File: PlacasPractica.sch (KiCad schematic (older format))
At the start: 70 parts

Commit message: Añadidos puertos
Puertos comunicaciones y sensores
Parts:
- removed 1M, 3M, R? (x6): R, symbol R
- removed C? (x5): CP, symbol CP
- removed C? (x4): C, symbol C
- removed D? (x2): D_Schottky, symbol D_Schottky
- removed D? (x3): D_Schottky_Small, symbol D_Schottky_Small
- removed J?: CONN_01X03_FEMALE, symbol CONN_01X03_FEMALE
- removed J? (x2): CONN_01X02_MALE, symbol CONN_01X02_MALE
- removed JP? (x2): Jumper_NC_Dual, symbol Jumper_NC_Dual
- removed Q? (x3): Q_PMOS_GDS, symbol Q_PMOS_GDS
- removed U?: MCP73831T-2ATI/OT, SOT95P300X145-5N, symbol MCP73831T-2ATI/OT
- removed U? (x3): XC6220B331MR-G, SOT95P300X145-5N, symbol XC6220B331MR-G
- added ADC? (x2), DIGITAL? (x2), ONEWIRE?: CONN_01x04, symbol CONN_01x04
- added C? (x3): C, symbol C
- added C? (x3): CP, symbol CP
- added D? (x3): D_Schottky_Small, symbol D_Schottky_Small
- added JP? (x2): Jumper_NC_Dual, symbol Jumper_NC_Dual
- added R? (x2): R, symbol R
- added U? (x3): XC6220B331MR-G, SOT95P300X145-5N, symbol XC6220B331MR-G
- renumbered 0.1uF to 0.1uF?, 4k7 to 4k?, i2c to I2C?, UART to UART?
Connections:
- net 3V3_SW is gone; now on net SCL: I2C?.1
- net 3v3_SW is gone; now on net OneWire: R?.1
- net +5V: now also D?.2 (A), D?.2 (A), D?.2 (A)
- net 3v3: no longer UART?.1
- net A0: now also ADC?.2
- net A1: now also ADC?.2
- net D0: now also DIGITAL?.2
- net D1: now also DIGITAL?.1
- net D2: now also DIGITAL?.2
- net D3: now also DIGITAL?.1
- net GND: now also D?.1 (K), I2C?.4, ADC?.4, ADC?.4, C?.2, C?.2, C?.2, C?.2, C?.2, C?.2, DIGITAL?.4, DIGITAL?.4, ONEWIRE?.4, R?.2, R?.2, U?.2 (GND), U?.2 (GND), U?.2 (GND); no longer I2C?.2
- net OneWire: now also U?.35 (GCLKIO2/TC2WO0/SERCOM3P0/SERCOM1P0/X4/PA16), ONEWIRE?.2; no longer R?.2
- net RXD: now also UART?.1; no longer UART?.3
- net SCL: no longer I2C?.3
- net SDA: now also I2C?.2; no longer I2C?.4
- net VCC_COM: now reaches U?.38 (ACCMP1/TC3WO1/SERCOM3P3/SERCOM1P3/X7/PA19)
- net VCC_COM: now also JP?.1
- net at JP?.1: now also R?.2
- net at R?.1: now also D?.2 (A); no longer JP?.2
- net 3v3_BEE renamed 3V3_COM
- net 3V3_COM: now also UART?.3, C?.1, DIGITAL?.3, DIGITAL?.3, U?.5 (VOUT)
- net BAT_VOLT: no longer names the net of U?.61 (PB00/AIN8/Y6/SERCOM5P2/TC7WO0)
- net BEE_VCC: no longer names the net of U?.53 (GCLKIO0/PA28)
- net VCC_SW renamed VCC_SENS
- net VCC_SENS: now also JP?.1
- new net: C?.1, D?.1 (K), JP?.2, U?.1 (VIN), U?.3 (CE)
- new net: C?.1, D?.1 (K), JP?.3, U?.1 (VIN) (x2)
- new net: JP?.2, R?.1, U?.3 (CE) (x2)
- new net 3V3: C?.1, U?.5 (VOUT)
- new net 3V3_SENS: ADC?.3, ADC?.3, C?.1, I2C?.3, ONEWIRE?.3, R?.2, U?.5 (VOUT)
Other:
- note added: "COMMUNICATION SWITCH"
- note added: "GENERAL 3V3"
- note added: "SENSOR SWITCH"
- note removed: "3v3"
- note removed: "BATT/SOLAR"
- note removed: "BEE SWITCH"
- note removed: "I/O SWITCH"
- note removed: "LiPo CHARGER"
- moved on the sheet: 0.1uF?, 4k?, D?, I2C?, J?, JP?, R?, U?, UART?

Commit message: Reset, Vddcore
Se  ha añadido el botón de reset y el jumper para la conexión de Vddcore en función del chip a usar.
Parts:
- added C?: 100nF, symbol C
- added JP?: Jumper_NC_Dual, symbol Jumper_NC_Dual
- added R?: 330, symbol R
- added R?: 10k, symbol R
- added SW?: SW_Push, symbol SW_Push
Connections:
- net 3V3: now also R?.1
- net GND: now also C?.2, SW?.2
- net RESETN: now also C?.1, R?.1, R?.2
- net Vddcore2: now reaches U?.53 (GCLKIO0/PA28)
- net Vddcore2: now also JP?.1
- net at C?.1: now also JP?.2; no longer U?.55 (VDDCORE)
- new net: R?.2, SW?.1
- new net Vddcore1: JP?.3, U?.55 (VDDCORE)
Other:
- note added: "Para D21\n"
- note added: "Para L21"
- note added: "Reset_button\n"
- note added: "Vddcore"
- moved on the sheet: C?
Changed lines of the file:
@@
 LIBS:contrib
 LIBS:valves
+LIBS:switches
 LIBS:PlacasPractica-cache
 EELAYER 25 0
@@
 L CP C?
 U 1 1 59060D19
-P 2050 1600
-F 0 "C?" H 2075 1700 50  0000 L CNN
-F 1 "CP" H 2075 1500 50  0000 L CNN
-F 2 "" H 2088 1450 50  0001 C CNN
-F 3 "" H 2050 1600 50  0001 C CNN
-	1    2050 1600
+P 9800 4800
+F 0 "C?" H 9825 4900 50  0000 L CNN
+F 1 "CP" H 9825 4700 50  0000 L CNN
+F 2 "" H 9838 4650 50  0001 C CNN
+F 3 "" H 9800 4800 50  0001 C CNN
+	1    9800 4800
 	-1   0    0    1
 $EndComp
@@
 L GND #PWR?
 U 1 1 59060D29
-P 2050 1400
-F 0 "#PWR?" H 2050 1150 50  0001 C CNN
-F 1 "GND" H 2050 1250 50  0000 C CNN
-F 2 "" H 2050 1400 50  0001 C CNN
-F 3 "" H 2050 1400 50  0001 C CNN
-	1    2050 1400
+P 9800 4600
+F 0 "#PWR?" H 9800 4350 50  0001 C CNN
+F 1 "GND" H 9800 4450 50  0000 C CNN
+F 2 "" H 9800 4600 50  0001 C CNN
+F 3 "" H 9800 4600 50  0001 C CNN
+	1    9800 4600
 	-1   0    0    1
 $EndComp
@@
 xBEE COM
 Wire Wire Line
-	2050 1400 2050 1450
+	9800 4600 9800 4650
 Wire Wire Line
 	2050 1750 2050 1800
@@
 Text Label 4400 3700 0    60   ~ 0
 OneWire
+$Comp
+L SW_Push SW?
+U 1 1 5AB3F66E
+P 7100 5850
+F 0 "SW?" H 7150 5950 50  0000 L CNN
+F 1 "SW_Push" H 7100 5790 50  0000 C CNN
+F 2 "" H 7100 6050 50  0001 C CNN
+F 3 "" H 7100 6050 50  0001 C CNN
+	1    7100 5850
+	0    1    1    0
+$EndComp
+$Comp
+L R R?
+U 1 1 5AB3FDE9
+P 7100 5350
+F 0 "R?" V 7180 5350 50  0000 C CNN
+F 1 "330" V 7100 5350 50  0000 C CNN
+F 2 "" V 7030 5350 50  0001 C CNN
+F 3 "" H 7100 5350 50  0001 C CNN
+	1    7100 5350
+	1    0    0    -1
+$EndComp
+$Comp
+L R R?
+U 1 1 5AB3FE8C
+P 7450 4700
+F 0 "R?" V 7530 4700 50  0000 C CNN
+F 1 "10k" V 7450 4700 50  0000 C CNN
+F 2 "" V 7380 4700 50  0001 C CNN
+F 3 "" H 7450 4700 50  0001 C CNN
+	1    7450 4700
+	1    0    0    -1
+$EndComp
+$Comp
+L C C?
+U 1 1 5AB3FF4F
+P 7700 5350
+F 0 "C?" H 7725 5450 50  0000 L CNN
+F 1 "100nF" H 7725 5250 50  0000 L CNN
+F 2 "" H 7738 5200 50  0001 C CNN
+F 3 "" H 7700 5350 50  0001 C CNN
+	1    7700 5350
+	1    0    0    -1
+$EndComp
+$Comp
+L GND #PWR?
+U 1 1 5AB40006
+P 7700 6100
+F 0 "#PWR?" H 7700 5850 50  0001 C CNN
+F 1 "GND" H 7700 5950 50  0000 C CNN
+F 2 "" H 7700 6100 50  0001 C CNN
+F 3 "" H 7700 6100 50  0001 C CNN
+	1    7700 6100
+	1    0    0    -1
+$EndComp
+$Comp
+L GND #PWR?
+U 1 1 5AB40094
+P 8050 6100
+F 0 "#PWR?" H 8050 5850 50  0001 C CNN
+F 1 "GND" H 8050 5950 50  0000 C CNN
+F 2 "" H 8050 6100 50  0001 C CNN
+F 3 "" H 8050 6100 50  0001 C CNN
+	1    8050 6100
+	0    -1   -1   0
+$EndComp
+Wire Wire Line
+	7450 4850 7450 5200
+Wire Wire Line
+	7100 5200 8150 5200
+Connection ~ 7450 5200
+Wire Wire Line
+	7100 5500 7100 5650
+Wire Wire Line
+	7100 6050 7100 6100
+Wire Wire Line
+	7100 6100 8050 6100
+Connection ~ 7700 6100
+Wire Wire Line
+	7700 5500 7700 6100
+Text Label 7450 4550 1    60   ~ 0
+3V3
+Connection ~ 7700 5200
+Text Label 8150 5200 0    60   ~ 0
+RESETN
+Wire Notes Line
+	6700 4250 6700 6450
+Wire Notes Line
+	6700 6450 8650 6450
+Wire Notes Line
+	8650 6450 8650 4250
+Wire Notes Line
+	8650 4250 6700 4250
+Text Notes 7750 4550 0    60   ~ 0
+Reset_button\n
+Text Label 2050 1750 1    60   ~ 0
+Vddcore1
+Text Label 9550 5150 2    60   ~ 0
+Vddcore1
+Text Label 10100 5150 0    60   ~ 0
+Vddcore2
+$Comp
+L Jumper_NC_Dual JP?
+U 1 1 5AB4AF6E
+P 9800 5150
+F 0 "JP?" H 9850 5050 50  0000 L CNN
+F 1 "Jumper_NC_Dual" H 9800 5250 50  0000 C BNN
+F 2 "" H 9800 5150 50  0001 C CNN
+F 3 "" H 9800 5150 50  0001 C CNN
+	1    9800 5150
+	-1   0    0    1
+$EndComp
+Wire Wire Line
+	10100 5150 10050 5150
+Wire Wire Line
+	9800 4950 9800 5050
+Text Label 4400 4800 0    60   ~ 0
+Vddcore2
+Wire Notes Line
+	9000 4250 9000 5650
+Wire Notes Line
+	9000 5650 10650 5650
+Wire Notes Line
+	10650 5650 10650 4250
+Wire Notes Line
+	10650 4250 9000 4250
+Text Notes 10050 4500 0    60   ~ 0
+Vddcore
+Text Notes 10100 4950 0    60   ~ 0
+Para L21
+Text Notes 9150 5000 0    60   ~ 0
+Para D21\n
 $EndSCHEMATC

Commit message: Añadidos conectores genericos
Se han añadido los conectores genéricos
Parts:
- added J? (x2): Conn_01x10, symbol Conn_01x10
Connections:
- net 3V3: now also J?.2 (Pin_2), J?.9 (Pin_9)
- net A2: now also J?.3 (Pin_3)
- net A3: now also J?.4 (Pin_4)
- net A4: now also J?.5 (Pin_5)
- net A5: now also J?.6 (Pin_6)
- net A6: now also J?.7 (Pin_7)
- net A7: now also J?.8 (Pin_8)
- net A8: now also J?.9 (Pin_9)
- net A9: now also J?.10 (Pin_10)
- net D10: now also J?.2 (Pin_2)
- net D4: now also J?.8 (Pin_8)
- net D5: now also J?.7 (Pin_7)
- net D6: now also J?.6 (Pin_6)
- net D7: now also J?.5 (Pin_5)
- net D8: now also J?.4 (Pin_4)
- net D9: now also J?.3 (Pin_3)
- net GND: now also J?.1 (Pin_1), J?.10 (Pin_10)
- net D12: now reaches U?.36 (GCLKIO3/TC2WO1/SERCOM3P1/SERCOM1P1/X5/PA17)
- net D13: now reaches U?.37 (ACCMP0/TC3WO0/SERCOM3P2/SERCOM1P2/X6/PA18)
- net OneWire renamed D11
- net D11: now also J?.1 (Pin_1)
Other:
- note added: "CONECTORES DEDICADOS"
- note added: "CONECTORES GENERICOS"
- note removed: "CONECTORES"
- moved on the sheet: C?, JP?, R?, SW?

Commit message: Actualizado anotado
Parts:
- gave numbers to parts that had none: 64

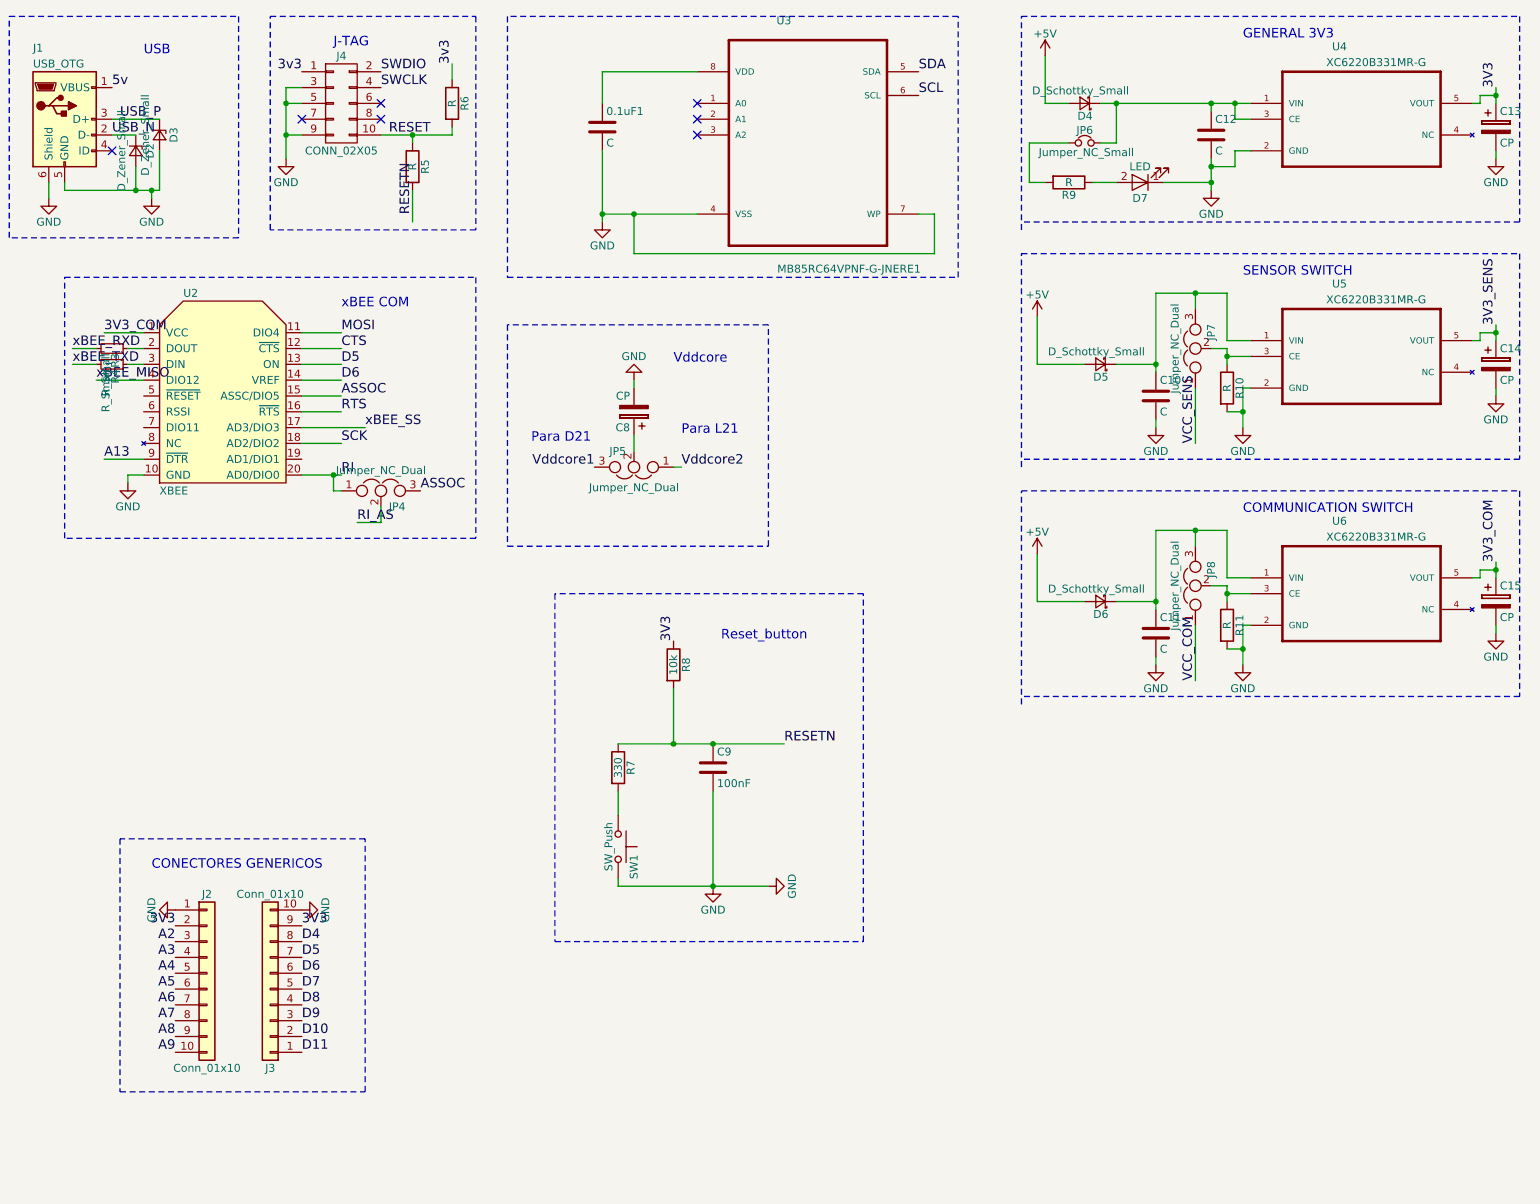
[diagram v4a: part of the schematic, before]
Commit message: Modificacion de la alimentación de Vddcore
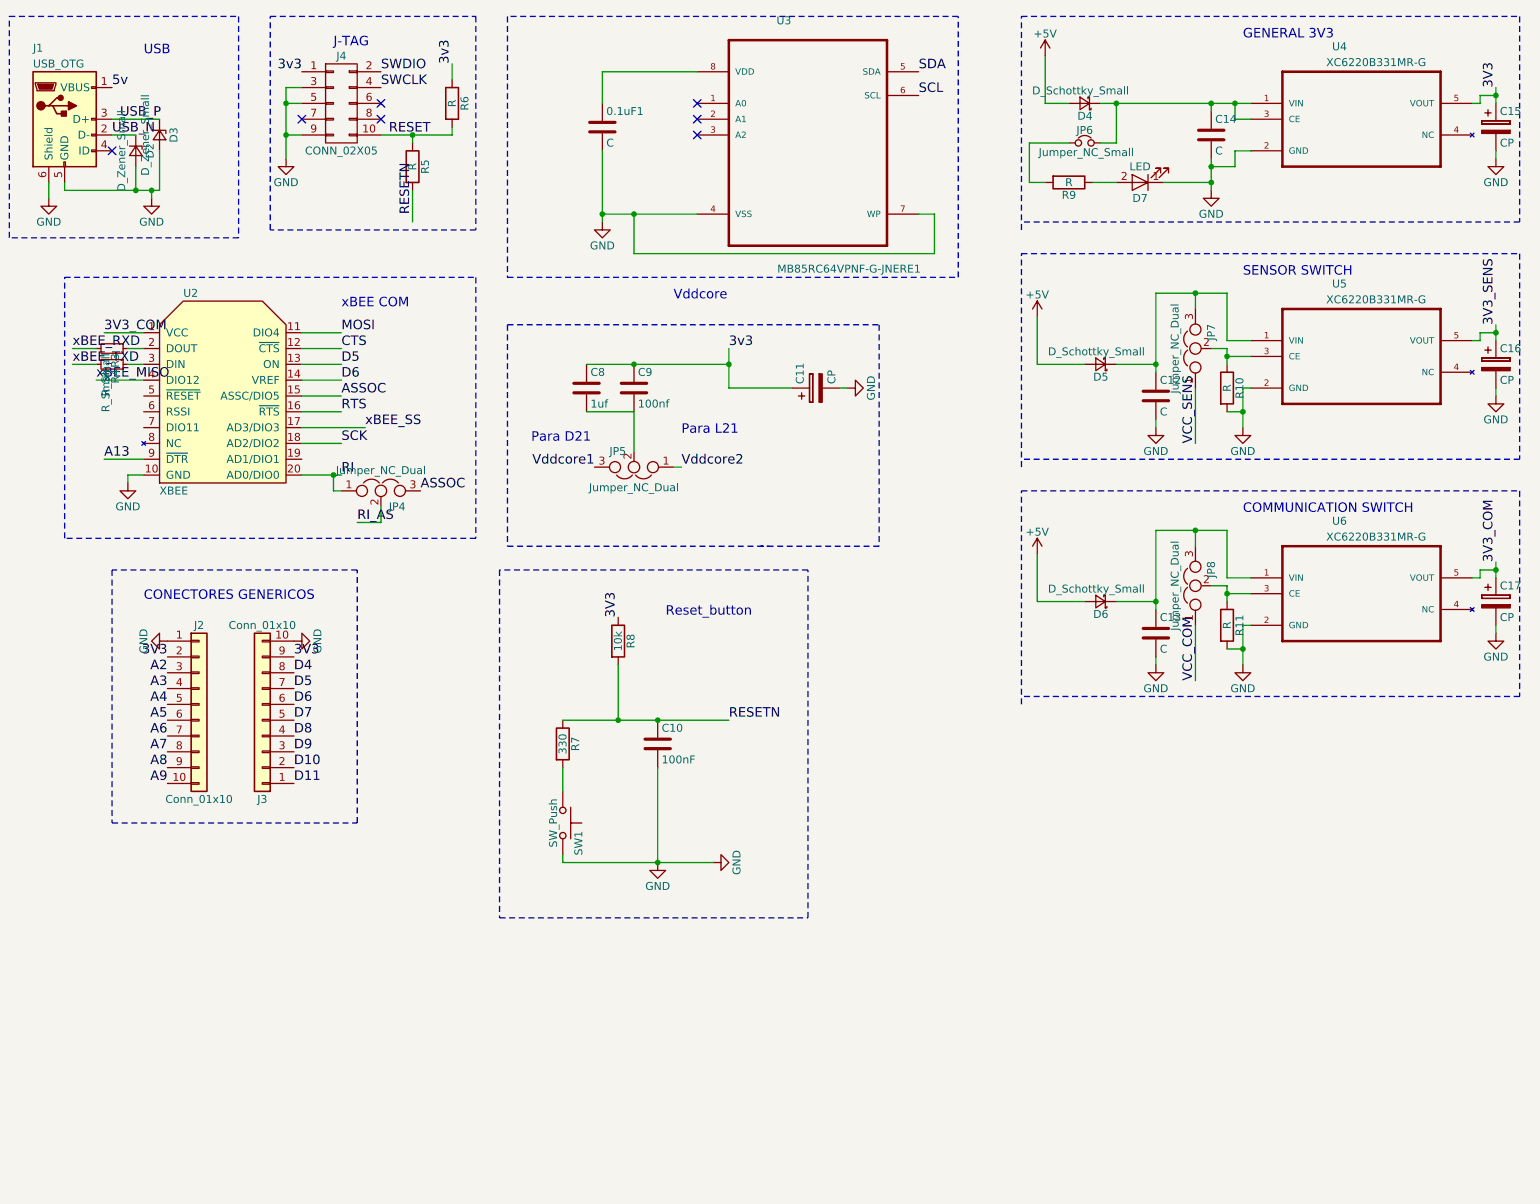
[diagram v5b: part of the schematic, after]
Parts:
- added C8: 1uf, symbol C
- added C9: 100nf, symbol C
- 0.1uF1, C1, C2, C3, C4, C5, C6, C7: footprint (none) -> Capacitors_SMD:C_1206_HandSoldering
- C14: renamed from C12; footprint (none) -> Capacitors_SMD:C_1206_HandSoldering
- renumbered C9 to C10, C8 to C11, C10 to C12, C11 to C13, C13 to C15, C14 to C16, C15 to C17
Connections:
- net 3v3: now also C11.1, C8.1, C9.1
- net at JP5.2: now also C8.2, C9.2; no longer C11.1
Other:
- moved on the sheet: C10, C11, J2, J3, R7, R8, SW1

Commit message: Huellas asignadas.
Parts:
- 4k1, 4k2, R1, R10, R11, R2, R3, R4, R5, R6, R7, R8, R9: footprint (none) -> Resistors_SMD:R_1812_HandSoldering
- ADC1, ADC2, DIGITAL1, DIGITAL2, I2C1, ONEWIRE1, UART1: footprint (none) -> Sockets_MOLEX_KK-System:Socket_MOLEX-KK-RM2-54mm_Lock_4pin_straight
- C10, C12, C13, C8, C9: footprint (none) -> Capacitors_SMD:C_1206_HandSoldering
- C11, C15, C16, C17: footprint (none) -> Capacitors_SMD:CP_Elec_6.3x5.8
- D1, D7: footprint (none) -> LEDs:LED_1206_HandSoldering
- D2, D3, D4, D5, D6: footprint (none) -> Diodes_SMD:D_SOD-323_HandSoldering
- J1: footprint (none) -> Connectors_USB:USB_Micro-B_Wuerth-629105150521_CircularHoles
- J2, J3: footprint (none) -> Pin_Headers:Pin_Header_Straight_1x10_Pitch1.27mm
- J4: footprint (none) -> Pin_Headers:Pin_Header_Straight_2x05_Pitch1.00mm
- JP1, JP6: footprint (none) -> jumper:SOLDER-JUMPER_1-WAY
- JP2, JP3, JP4, JP5, JP7, JP8: footprint (none) -> jumper:SOLDER-JUMPER_2-WAY
- L1: footprint (none) -> Inductors:Inductor_Taiyo-Yuden_NR-60xx_HandSoldering
- SW1: footprint (none) -> Buttons_Switches_SMD:SW_SPST_B3U-1000P
- Y1: footprint (none) -> Crystals:Crystal_SMD_0603-2pin_6.0x3.5mm_HandSoldering

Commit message: Huella Xbee incorporada
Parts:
- U2: footprint agg-unchecked:XBEE -> XBEE:XBEE
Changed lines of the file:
@@
 LIBS:valves
 LIBS:switches
+LIBS:ICs
 LIBS:PlacasPractica-cache
 EELAYER 25 0
@@
 F 0 "U2" H 7500 3650 50  0000 L CNN
 F 1 "XBEE" H 7350 2400 50  0000 L CNN
-F 2 "agg-unchecked:XBEE" H 7350 2300 50  0001 L CNN
+F 2 "XBEE:XBEE" H 7350 2300 50  0001 L CNN
 F 3 "" H 7250 3400 50  0001 C CNN
 	1    7750 3000
